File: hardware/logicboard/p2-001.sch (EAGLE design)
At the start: 64 parts, among them IC1 74LS07N, IC11 74LS153D, IC12 LTC485S, IC13 LTC485S, IC2 4066N, J1 MKR, J11 Qwiic, J12 Qwiic, J13 Qwiic, J14 Qwiic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

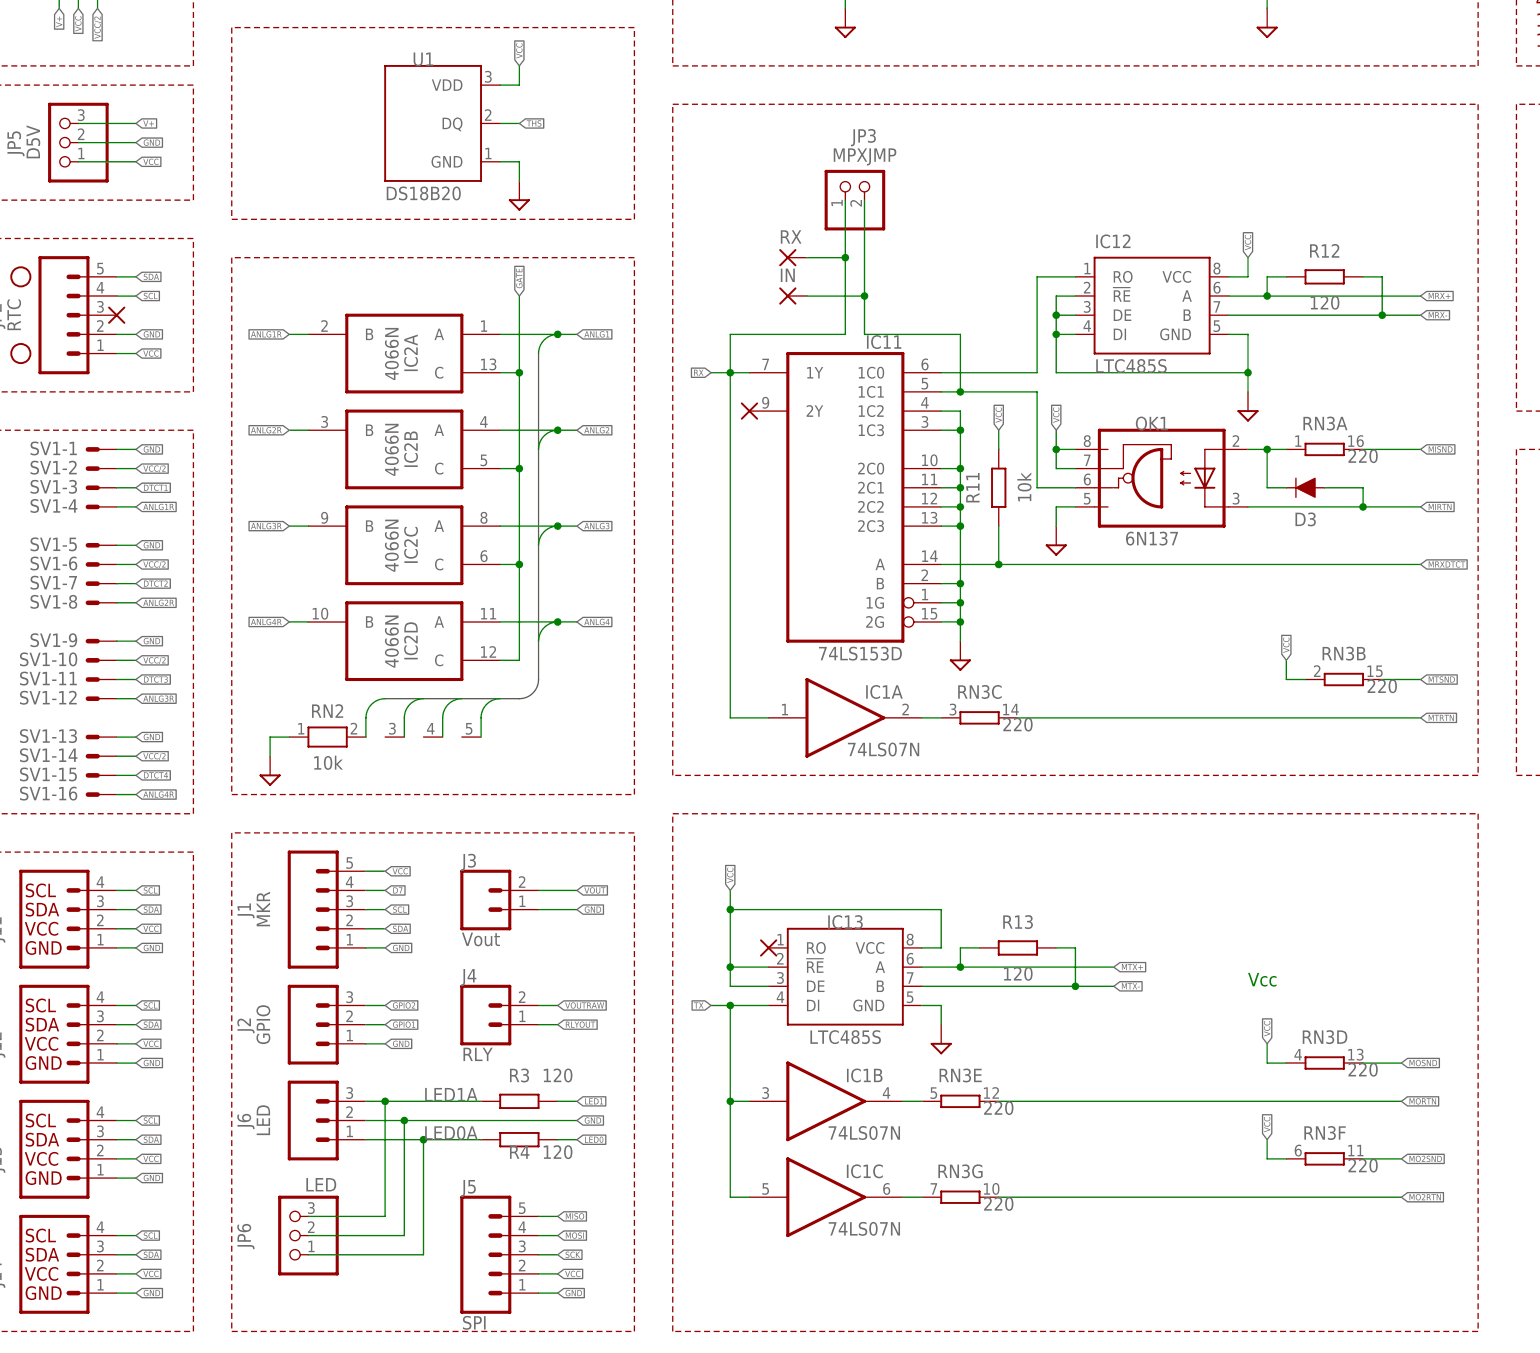
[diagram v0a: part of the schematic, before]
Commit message: JP5 is now compatible with Euroblock.
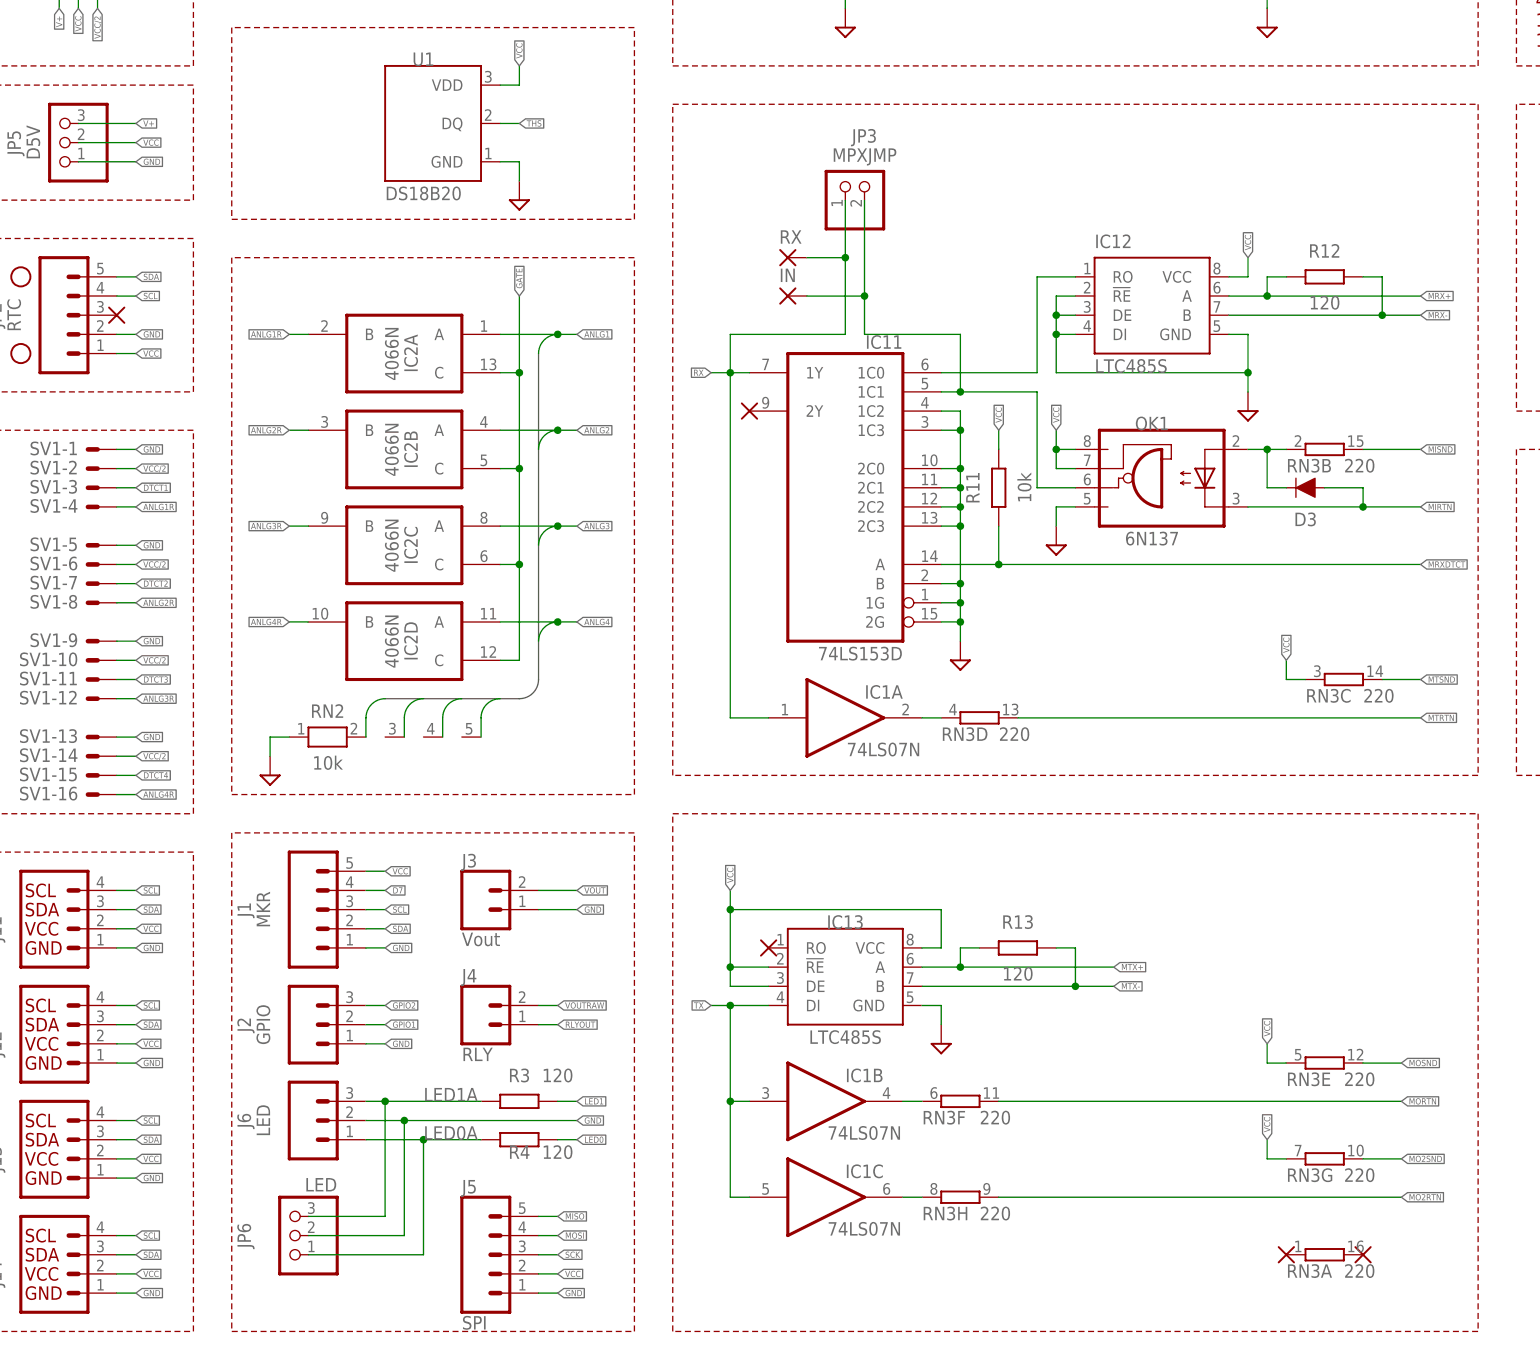
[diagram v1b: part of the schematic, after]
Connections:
- net GND: now also JP5.1; no longer JP5.2
- net MIDIINSND: now also RN3B.1; no longer RN3A.1
- net MISND: now also RN3B.2; no longer RN3A.2
- net MO: now also RN3F.1; no longer RN3E.1
- net MO2: now also RN3H.1; no longer RN3G.1
- net MO2RTN: now also RN3H.2; no longer RN3G.2
- net MO2SND: now also RN3G.2; no longer RN3F.2
- net MORTN: now also RN3F.2; no longer RN3E.2
- net MOSND: now also RN3E.2; no longer RN3D.2
- net MT: now also RN3D.1; no longer RN3C.1
- net MTRTN: now also RN3D.2; no longer RN3C.2
- net MTSND: now also RN3C.2; no longer RN3B.2
- net VCC: now also JP5.2, RN3C.1, RN3E.1, RN3G.1; no longer JP5.1, RN3B.1, RN3D.1, RN3F.1
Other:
- note removed: "Vcc"
- moved on the sheet: RN3A, RN3B, RN3C, RN3D, RN3E, RN3F, RN3G

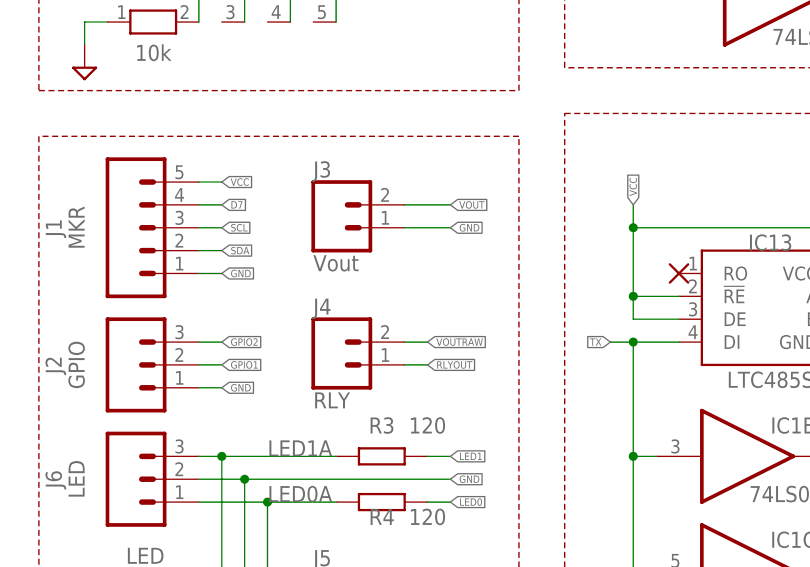
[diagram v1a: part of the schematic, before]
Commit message: Moved relay port.
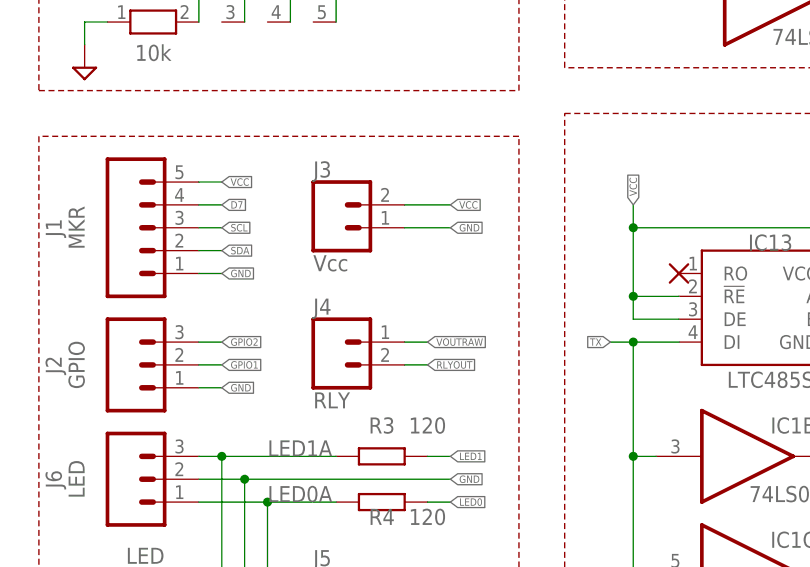
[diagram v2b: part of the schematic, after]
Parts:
- J3: value Vout -> Vcc
- J4: device SparkFun-Connectors:CONN_02JST-PTH-2 -> SparkFun-Connectors:CONN_02-JST-2MM-SMT
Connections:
- net VCC: now also J3.2
- net VOUT: no longer J3.2
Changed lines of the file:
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@@
 <part name="IN" library="wirepad" library_urn="urn:adsk.eagle:library:412" deviceset="SMD2" device="" package3d_urn="urn:adsk.eagle:package:30839/1"/>
 <part name="JP6" library="pinhead" library_urn="urn:adsk.eagle:library:325" deviceset="PINHD-1X3" device="" package3d_urn="urn:adsk.eagle:package:22458/2" value="LED"/>
-<part name="J4" library="SparkFun-Connectors" library_urn="urn:adsk.eagle:library:513" deviceset="CONN_02" device="JST-PTH-2" package3d_urn="urn:adsk.eagle:package:38053/1" value="RLY"/>
-<part name="J3" library="SparkFun-Connectors" library_urn="urn:adsk.eagle:library:513" deviceset="CONN_02" device="JST-PTH-2" package3d_urn="urn:adsk.eagle:package:38053/1" value="Vout"/>
+<part name="J4" library="SparkFun-Connectors" library_urn="urn:adsk.eagle:library:513" deviceset="CONN_02" device="-JST-2MM-SMT" package3d_urn="urn:adsk.eagle:package:38042/1" value="RLY"/>
+<part name="J3" library="SparkFun-Connectors" library_urn="urn:adsk.eagle:library:513" deviceset="CONN_02" device="JST-PTH-2" package3d_urn="urn:adsk.eagle:package:38053/1" value="Vcc"/>
 <part name="J5" library="SparkFun-Connectors" library_urn="urn:adsk.eagle:library:513" deviceset="CONN_05" device="JST-VERT" package3d_urn="urn:adsk.eagle:package:38111/1" value="SPI"/>
 <part name="RN3" library="resistor-dil" library_urn="urn:adsk.eagle:library:342" deviceset="8R-N" device="" package3d_urn="urn:adsk.eagle:package:922/2" value="220"/>
@@
 <label x="43.18" y="165.1" size="0.8128" layer="95" xref="yes"/>
 </segment>
+<segment>
+<wire x1="96.52" y1="66.04" x2="101.6" y2="66.04" width="0.1524" layer="91"/>
+<pinref part="J3" gate="G$1" pin="2"/>
+<label x="101.6" y="66.04" size="0.8128" layer="95" xref="yes"/>
+</segment>
 </net>
 <net name="MIDIINSND" class="0">
@@
 <label x="38.1" y="205.74" size="0.8128" layer="95" rot="R90" xref="yes"/>
 </segment>
-<segment>
-<wire x1="96.52" y1="66.04" x2="101.6" y2="66.04" width="0.1524" layer="91"/>
-<pinref part="J3" gate="G$1" pin="2"/>
-<label x="101.6" y="66.04" size="0.8128" layer="95" xref="yes"/>
-</segment>
-</net>
+</net>

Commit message: First try.
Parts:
- added RN4: 10k, resistor-net:RN04
- IC1: value 74LS07N -> 74LS06N; device 74xx-us:74LS07N -> 74xx-us:74LS06N
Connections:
- removed net MO: IC1B.O, RN3F.1
- removed net MO2: IC1C.O, RN3H.1
- removed net MT: IC1A.O, RN3D.1
- new net MO2RTNRAW: IC1F.O, RN3H.1
- new net MORTNRAW: IC1E.O, RN3F.1
- new net MTRTNRAW: IC1D.O, RN3D.1
- new net NMO2RTN: IC1C.O, IC1F.I, RN4.4
- new net NMORTN: IC1B.O, IC1E.I, RN4.3
- new net NMTRTN: IC1A.O, IC1D.I, RN4.2
- net GND: no longer IC1D.I, IC1E.I, IC1F.I
- net VCC: now also RN4.1
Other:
- moved on the sheet: RN3D, RN3F, RN3H

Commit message: Second try.
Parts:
- RN4: value 10k -> 4.7k
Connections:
- net NMO2RTN: now also RN1.5; no longer RN4.4
- net NMORTN: now also RN1.4; no longer RN4.3
- net NMTRTN: now also RN1.3; no longer RN4.2
- net SCL: now also RN4.3; no longer RN1.4
- net SDA: now also RN4.2; no longer RN1.3
- net THS: now also RN4.4; no longer RN1.5
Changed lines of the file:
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@@
 <part name="X5" library="wirepad" library_urn="urn:adsk.eagle:library:412" deviceset="PAD-N" device=""/>
 <part name="X8" library="wirepad" library_urn="urn:adsk.eagle:library:412" deviceset="PAD-N" device=""/>
-<part name="RN4" library="resistor-net" library_urn="urn:adsk.eagle:library:343" deviceset="RN04" device="" package3d_urn="urn:adsk.eagle:package:24976/1" value="10k"/>
+<part name="RN4" library="resistor-net" library_urn="urn:adsk.eagle:library:343" deviceset="RN04" device="" package3d_urn="urn:adsk.eagle:package:24976/1" value="4.7k"/>
 <part name="X1" library="wirepad" library_urn="urn:adsk.eagle:library:412" deviceset="PAD-N" device=""/>
 </parts>
@@
 </segment>
 <segment>
-<pinref part="RN1" gate="1" pin="5"/>
-<wire x1="251.46" y1="134.62" x2="254" y2="134.62" width="0.1524" layer="91"/>
-<label x="254" y="134.62" size="0.8128" layer="95" xref="yes"/>
-</segment>
-<segment>
 <pinref part="U1" gate="G$1" pin="DQ"/>
 <wire x1="91.44" y1="167.64" x2="93.98" y2="167.64" width="0.1524" layer="91"/>
 <label x="93.98" y="167.64" size="0.8128" layer="95" xref="yes"/>
+</segment>
+<segment>
+<pinref part="RN4" gate="1" pin="4"/>
+<wire x1="233.68" y1="139.7" x2="236.22" y2="139.7" width="0.1524" layer="91"/>
+<label x="236.22" y="139.7" size="0.8128" layer="95" xref="yes"/>
 </segment>
 </net>
@@
 </segment>
 <segment>
-<pinref part="RN1" gate="1" pin="3"/>
-<wire x1="251.46" y1="144.78" x2="254" y2="144.78" width="0.1524" layer="91"/>
-<label x="254" y="144.78" size="0.8128" layer="95" xref="yes"/>
-</segment>
-<segment>
 <pinref part="J1" gate="G$1" pin="2"/>
 <wire x1="73.66" y1="60.96" x2="76.2" y2="60.96" width="0.1524" layer="91"/>
@@
 <label x="43.18" y="17.78" size="0.8128" layer="95" xref="yes"/>
 </segment>
+<segment>
+<pinref part="RN4" gate="1" pin="2"/>
+<wire x1="233.68" y1="149.86" x2="236.22" y2="149.86" width="0.1524" layer="91"/>
+<label x="236.22" y="149.86" size="0.8128" layer="95" xref="yes"/>
+</segment>
 </net>
 <net name="SCL" class="0">
@@
 </segment>
 <segment>
-<pinref part="RN1" gate="1" pin="4"/>
-<wire x1="251.46" y1="139.7" x2="254" y2="139.7" width="0.1524" layer="91"/>
-<label x="254" y="139.7" size="0.8128" layer="95" xref="yes"/>
-</segment>
-<segment>
 <pinref part="J1" gate="G$1" pin="3"/>
 <wire x1="73.66" y1="63.5" x2="76.2" y2="63.5" width="0.1524" layer="91"/>
@@
 <wire x1="40.64" y1="20.32" x2="43.18" y2="20.32" width="0.1524" layer="91"/>
 <label x="43.18" y="20.32" size="0.8128" layer="95" xref="yes"/>
+</segment>
+<segment>
+<pinref part="RN4" gate="1" pin="3"/>
+<wire x1="233.68" y1="144.78" x2="236.22" y2="144.78" width="0.1524" layer="91"/>
+<label x="236.22" y="144.78" size="0.8128" layer="95" xref="yes"/>
 </segment>
 </net>
@@
 </segment>
 <segment>
-<pinref part="RN4" gate="1" pin="2"/>
-<wire x1="233.68" y1="149.86" x2="236.22" y2="149.86" width="0.1524" layer="91"/>
-<label x="236.22" y="149.86" size="0.8128" layer="95" xref="yes"/>
+<pinref part="RN1" gate="1" pin="3"/>
+<wire x1="251.46" y1="144.78" x2="254" y2="144.78" width="0.1524" layer="91"/>
+<label x="254" y="144.78" size="0.8128" layer="95" xref="yes"/>
 </segment>
 </net>
@@
 </segment>
 <segment>
-<pinref part="RN4" gate="1" pin="3"/>
-<wire x1="233.68" y1="144.78" x2="236.22" y2="144.78" width="0.1524" layer="91"/>
-<label x="236.22" y="144.78" size="0.8128" layer="95" xref="yes"/>
+<pinref part="RN1" gate="1" pin="4"/>
+<wire x1="251.46" y1="139.7" x2="254" y2="139.7" width="0.1524" layer="91"/>
+<label x="254" y="139.7" size="0.8128" layer="95" xref="yes"/>
 </segment>
 </net>
@@
 </segment>
 <segment>
-<pinref part="RN4" gate="1" pin="4"/>
-<wire x1="233.68" y1="139.7" x2="236.22" y2="139.7" width="0.1524" layer="91"/>
-<label x="236.22" y="139.7" size="0.8128" layer="95" xref="yes"/>
-</segment>
-</net>
+<pinref part="RN1" gate="1" pin="5"/>
+<wire x1="251.46" y1="134.62" x2="254" y2="134.62" width="0.1524" layer="91"/>
+<label x="254" y="134.62" size="0.8128" layer="95" xref="yes"/>
+</segment>
+</net>
